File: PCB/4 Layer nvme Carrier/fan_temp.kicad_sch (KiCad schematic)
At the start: 20 parts, among them M1 Fan_4pin, M2 Fan_4pin

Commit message: Prototyp_1
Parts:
- JP2: now fitted
- R63: footprint Resistor_SMD:R_0402_1005Metric -> A_HDJ_Library:R_0402_1005Metric; MPN (none) -> RC0402FR-0710KL; now fitted; now in the parts list
- R64, R65: footprint Resistor_SMD:R_0402_1005Metric -> A_HDJ_Library:R_0402_1005Metric; MPN (none) -> RC0402FR-074K7L
- R66: footprint Resistor_SMD:R_0402_1005Metric -> A_HDJ_Library:R_0402_1005Metric; MPN (none) -> RC0402FR-0721K5L
- R67, R70, R71, R74: footprint Resistor_SMD:R_0402_1005Metric -> A_HDJ_Library:R_0402_1005Metric
- TH1: MPN (none) -> NCU18XH103F60RB; now fitted; now in the parts list
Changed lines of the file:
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@@
 			)
 		)
-		(property "Footprint" "Resistor_SMD:R_0402_1005Metric"
+		(property "Footprint" "A_HDJ_Library:R_0402_1005Metric"
 			(at 332.74 245.618 90)
 			(effects
@@
 		(at 213.36 158.75 0)
 		(unit 1)
-		(exclude_from_sim yes)
+		(exclude_from_sim no)
 		(in_bom no)
-		(on_board no)
-		(dnp yes)
+		(on_board yes)
+		(dnp no)
 		(fields_autoplaced yes)
 		(property "Reference" "JP2"
@@
 			)
 		)
-		(property "Footprint" "Resistor_SMD:R_0402_1005Metric"
+		(property "Footprint" "A_HDJ_Library:R_0402_1005Metric"
 			(at 311.912 173.99 90)
 			(effects
@@
 			)
 		)
-		(property "Datasheet" "~"
+		(property "Datasheet" "https://wmsc.lcsc.com/wmsc/upload/file/pdf/v2/lcsc/2304140030_YAGEO-RC0402FR-0721K5L_C185442.pdf"
 			(at 313.69 173.99 0)
 			(effects
@@
 		)
 		(property "Part#" ""
+			(at 313.69 173.99 0)
+			(effects
+				(font
+					(size 1.27 1.27)
+				)
+				(hide yes)
+			)
+		)
+		(property "MPN" "RC0402FR-0721K5L"
 			(at 313.69 173.99 0)
 			(effects
@@
 		(unit 1)
 		(exclude_from_sim no)
-		(in_bom no)
-		(on_board no)
-		(dnp yes)
+		(in_bom yes)
+		(on_board yes)
+		(dnp no)
 		(fields_autoplaced yes)
 		(property "Reference" "TH1"
@@
 			)
 		)
-		(property "Datasheet" "~"
+		(property "Datasheet" "https://www.mouser.de/datasheet/2/281/NCU18XH103F60RB-1519762.pdf"
 			(at 226.06 163.83 0)
 			(effects
@@
 		)
 		(property "Part#" ""
+			(at 226.06 165.1 0)
+			(effects
+				(font
+					(size 1.27 1.27)
+				)
+				(hide yes)
+			)
+		)
+		(property "MPN" " NCU18XH103F60RB "
 			(at 226.06 165.1 0)
 			(effects
@@
 			)
 		)
-		(property "Footprint" "Resistor_SMD:R_0402_1005Metric"
+		(property "Footprint" "A_HDJ_Library:R_0402_1005Metric"
 			(at 300.482 152.4 90)
 			(effects
@@
 			)
 		)
-		(property "Datasheet" "~"
+		(property "Datasheet" "https://wmsc.lcsc.com/wmsc/upload/file/pdf/v2/lcsc/2304140030_YAGEO-RC0402FR-074K7L_C105871.pdf"
 			(at 302.26 152.4 0)
 			(effects
@@
 		)
 		(property "Part#" ""
+			(at 302.26 152.4 0)
+			(effects
+				(font
+					(size 1.27 1.27)
+				)
+				(hide yes)
+			)
+		)
+		(property "MPN" "RC0402FR-074K7L"
 			(at 302.26 152.4 0)
 			(effects
@@
 			)
 		)
-		(property "Footprint" "Resistor_SMD:R_0402_1005Metric"
+		(property "Footprint" "A_HDJ_Library:R_0402_1005Metric"
 			(at 332.74 240.538 90)
 			(effects
@@
 			)
 		)
-		(property "Footprint" "Resistor_SMD:R_0402_1005Metric"
+		(property "Footprint" "A_HDJ_Library:R_0402_1005Metric"
 			(at 300.482 228.6 90)
 			(effects
@@
 			)
 		)
-		(property "Datasheet" "~"
+		(property "Datasheet" "https://wmsc.lcsc.com/wmsc/upload/file/pdf/v2/lcsc/2304140030_YAGEO-RC0402FR-074K7L_C105871.pdf"
 			(at 302.26 228.6 0)
 			(effects
@@
 		)
 		(property "Part#" ""
+			(at 302.26 228.6 0)
+			(effects
+				(font
+					(size 1.27 1.27)
+				)
+				(hide yes)
+			)
+		)
+		(property "MPN" "RC0402FR-074K7L"
 			(at 302.26 228.6 0)
 			(effects
@@
 		(unit 1)
 		(exclude_from_sim no)
-		(in_bom no)
-		(on_board no)
-		(dnp yes)
+		(in_bom yes)
+		(on_board yes)
+		(dnp no)
 		(property "Reference" "R63"
 			(at 227.33 153.67 0)
@@
 			)
 		)
-		(property "Footprint" "Resistor_SMD:R_0402_1005Metric"
+		(property "Footprint" "A_HDJ_Library:R_0402_1005Metric"
 			(at 224.282 152.4 90)
 			(effects
@@
 			)
 		)
-		(property "Datasheet" "~"
+		(property "Datasheet" "https://wmsc.lcsc.com/wmsc/upload/file/pdf/v2/lcsc/2304140030_YAGEO-RC0402FR-0710KL_C60490.pdf"
 			(at 226.06 152.4 0)
 			(effects
@@
 		)
 		(property "Part#" ""
+			(at 226.06 152.4 0)
+			(effects
+				(font
+					(size 1.27 1.27)
+				)
+				(hide yes)
+			)
+		)
+		(property "MPN" "RC0402FR-0710KL"
 			(at 226.06 152.4 0)
 			(effects
@@
 			)
 		)
-		(property "Footprint" "Resistor_SMD:R_0402_1005Metric"
+		(property "Footprint" "A_HDJ_Library:R_0402_1005Metric"
 			(at 311.912 250.19 90)
 			(effects
@@
 			)
 		)
-		(property "Footprint" "Resistor_SMD:R_0402_1005Metric"
+		(property "Footprint" "A_HDJ_Library:R_0402_1005Metric"
 			(at 351.282 228.6 90)
 			(effects

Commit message: Silk and BOM changes
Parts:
- C84: LCSC Part # (none) -> C77020; Package (none) -> 0402; Part# (none) -> C77020
- C85: footprint Capacitor_SMD:C_0402_1005Metric -> A_HDJ_Library:C_0402_1005Metric; LCSC Part # (none) -> C77020; Package (none) -> 0402; Part# (none) -> C77020
- D26, D27: LCSC Part # (none) -> C2828425; Package (none) -> SOD-323; Part# (none) -> C2828425
- JP2: Package (none) -> SolderJumper; now in the parts list
- M1: LCSC Part # (none) -> C566011; Package (none) -> Plugin,P=2mm; Part# (none) -> C566011
- M2: LCSC Part # (none) -> C240840; Package (none) -> Plugin,P=2.54mm; Part# (none) -> C240840
- R63: LCSC Part # (none) -> C60490; Package (none) -> 0402; Part# (none) -> C60490
- R64, R65, R72, R74: LCSC Part # (none) -> C105871; Package (none) -> 0402; Part# (none) -> C105871
- R66, R67, R68, R70: LCSC Part # (none) -> C185442; Package (none) -> 0402; Part# (none) -> C185442
- R69, R71: LCSC Part # (none) -> C106232; Package (none) -> 0402; Part# (none) -> C106232
- TH1: LCSC Part # (none) -> C440252; MPN NCU18XH103F60RB -> NCU18XH103F60RB; Package (none) -> 0603; Part# (none) -> C440252

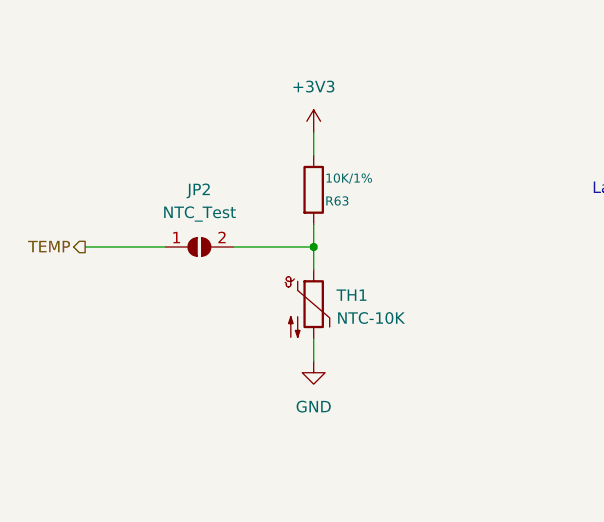
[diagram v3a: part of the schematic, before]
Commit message: new JPG, new 3V3 names and del the M.2 60mm mounts
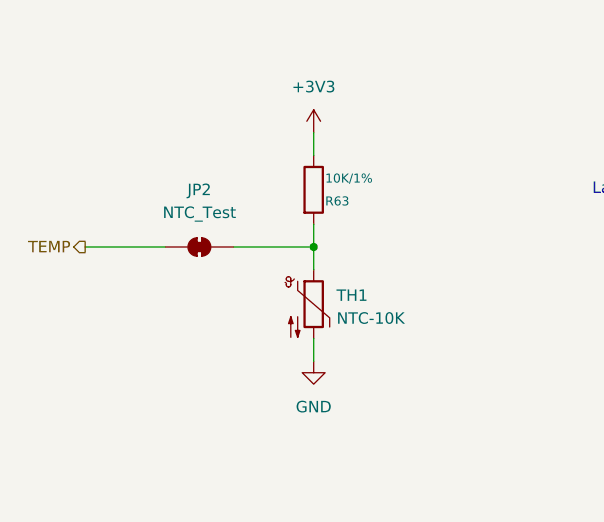
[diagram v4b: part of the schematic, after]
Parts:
- JP2: footprint Jumper:SolderJumper-2_P1.3mm_Open_RoundedPad1.0x1.5mm -> Jumper:SolderJumper-2_P1.3mm_Bridged_RoundedPad1.0x1.5mm; symbol Jumper:SolderJumper_2_Open -> Jumper:SolderJumper_2_Bridged; now left out of the parts list
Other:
- moved on the sheet: JP2
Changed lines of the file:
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@@
 	)
 	(symbol
-		(lib_id "Jumper:SolderJumper_2_Open")
+		(lib_id "Jumper:SolderJumper_2_Bridged")
 		(at 213.36 158.75 0)
 		(unit 1)
-		(exclude_from_sim no)
-		(in_bom yes)
+		(exclude_from_sim yes)
+		(in_bom no)
 		(on_board yes)
 		(dnp no)
@@
 			)
 		)
-		(property "Footprint" "Jumper:SolderJumper-2_P1.3mm_Open_RoundedPad1.0x1.5mm"
+		(property "Footprint" "Jumper:SolderJumper-2_P1.3mm_Bridged_RoundedPad1.0x1.5mm"
 			(at 213.36 158.75 0)
 			(effects
@@
 			)
 		)
-		(property "Description" ""
+		(property "Description" "Solder Jumper, 2-pole, closed/bridged"
 			(at 213.36 158.75 0)
 			(effects
